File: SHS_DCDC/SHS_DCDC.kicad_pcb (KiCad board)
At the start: 6 copper layers, 100 x 100 mm, 130 parts, among them J1 Barrel_Jack, J2 USB_A, J3 Conn_ARM_JTAG_SWD_10, J4 Conn_01x02_Male, Q1 BSS84, Q10 PMV100XPEAR, Q11 PMV100XPEAR, Q12 PMV100XPEAR, Q13 PMV100XPEAR, Q14 PMV100XPEAR, Q15 BSS84, Q16 PMV100XPEAR, Q17 PMV100XPEAR, Q18 BSS84, Q19 2N7002, Q2 PMV100XPEAR, Q20 BSS84, Q21 2N7002, Q3 2N7002, Q4 2N7002, Q5 PMV100XPEAR, Q6 2N7002, Q7 PMV100XPEAR, Q8 Q_PMOS_DGS, Q9 PMV100XPEAR, U1 RT8299-WDFN10L, U2 INA181, U3 LMV324AIDR, U4 LMV358IDR, U5 MP3414A, U6 ESP32-S2-MINI-1, U7 MCP101, U8 MIC5501-3.0YM5, U9 BD49LxxG, Y1 2-SMD no lead

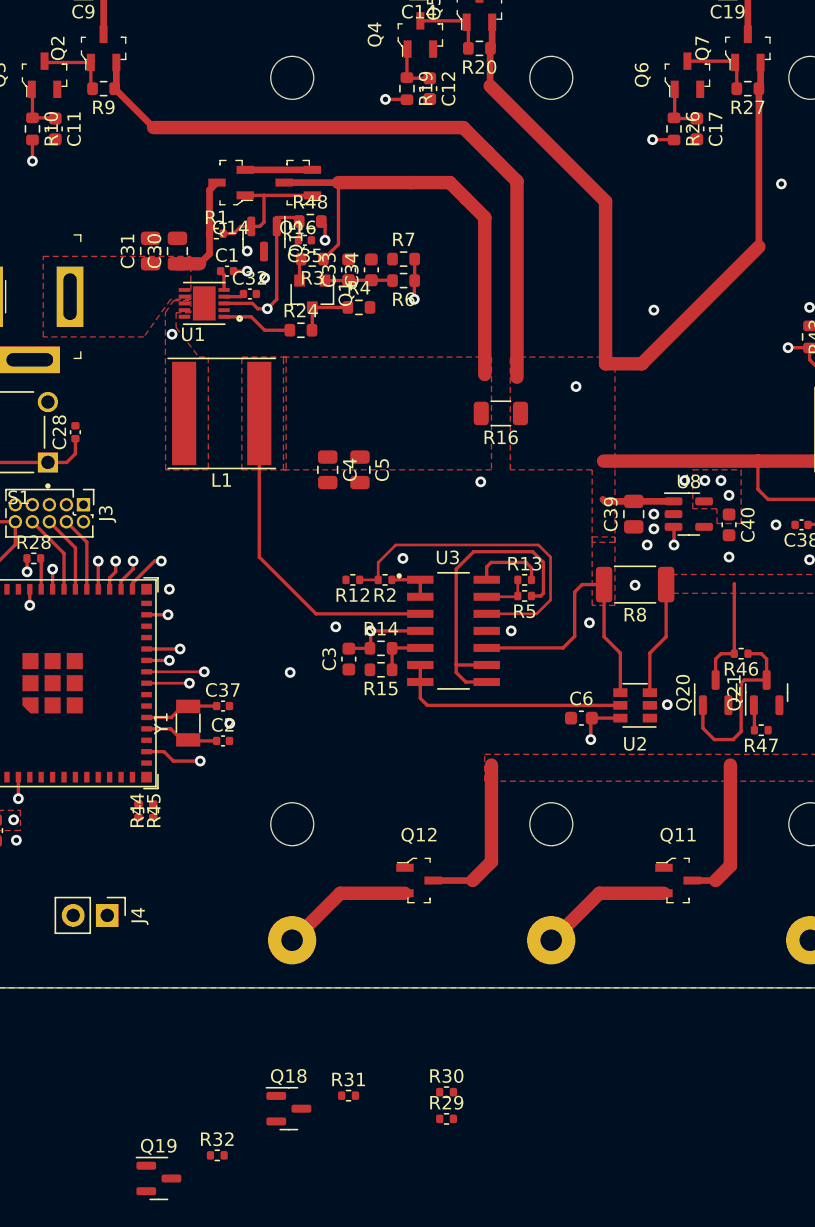
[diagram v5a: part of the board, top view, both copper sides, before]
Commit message: ADC_PV & BAT
Blocks related to ADC reading of PV and BAT added on the physical board.
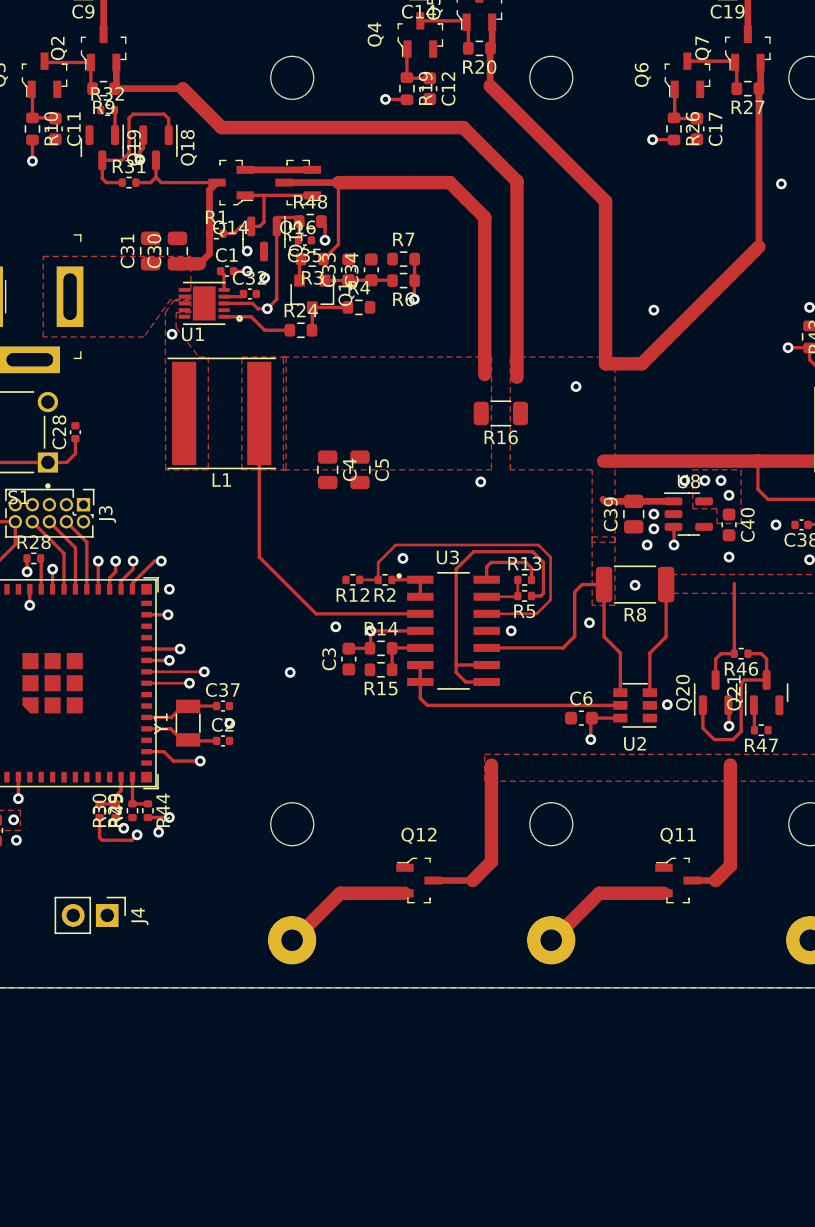
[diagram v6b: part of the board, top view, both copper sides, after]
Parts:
- moved R32 78.3 mm to (16.8, 34.6)
- moved Q19 76.9 mm to (16.4, 37.4), turned to -90 degrees
- moved Q18 72.3 mm to (20.4, 37.4), turned to -90 degrees
- moved R31 70.0 mm to (18.4, 40.0)
- moved R29 34.6 mm to (16.2, 86.8), turned to -90 degrees
- moved R30 32.4 mm to (17.4, 86.8), turned to 90 degrees
- moved R45 0.45 mm to (18.6, 86.8), turned to 90 degrees
- moved R44 0.40 mm to (19.8, 86.8), turned to -90 degrees
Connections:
- U2 pad 1: MCU_ADC_BAT -> MCU_ADC_IBAT
- U6 pad 14: unconnected-(U6-Pad14) -> MCU_ADC_PV
- U6 pad 15: unconnected-(U6-Pad15) -> MCU_ADC_BAT
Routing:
- net Net-(Q18-Pad2): track 0.00 -> 57.0 mm, vias 0 -> 2
- net Net-(Q20-Pad2): track 0.00 -> 47.6 mm, vias 0 -> 2
- net Net-(Q18-Pad1): track 0.00 -> 12.2 mm
- net PV: track 8.24 -> 15.9 mm
- net MCU_OCP_BAT: track 82.3 -> 85.8 mm
- net MCU_ADC_PV: track 0.00 -> 3.36 mm
- net MCU_ADC_BAT: track 0.00 -> 3.24 mm
- net MCU_ADC_PV_CTRL: track 0.00 -> 1.88 mm
- net GND: vias 44 -> 46
